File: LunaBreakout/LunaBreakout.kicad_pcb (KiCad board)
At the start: 2 copper layers, 62 parts, among them J1 Conn_01x03, J10 Conn_01x02, J11 Conn_01x03, J12 Conn_01x03, J13 Conn_01x04, J14 Conn_01x04, J15 5 V BEC, J16 GND, J17 Conn_01x04, J18 Conn_01x04, J19 Conn_01x04, J2 Conn_01x03, J3 Conn_01x04, J4 Conn_01x03, J5 Conn_01x03, J6 USB_C_Receptacle_USB2.0_16P, J8 Conn_01x04, J9 Conn_01x04, SW1 SW_SPST, U1 RP2040, U2 AMS1117-3.3, U3 W25Q32JVSS, U4 ISO7721D, U5 ISO7720D, U8 ISO7741DBQ, Y1 12Mhz

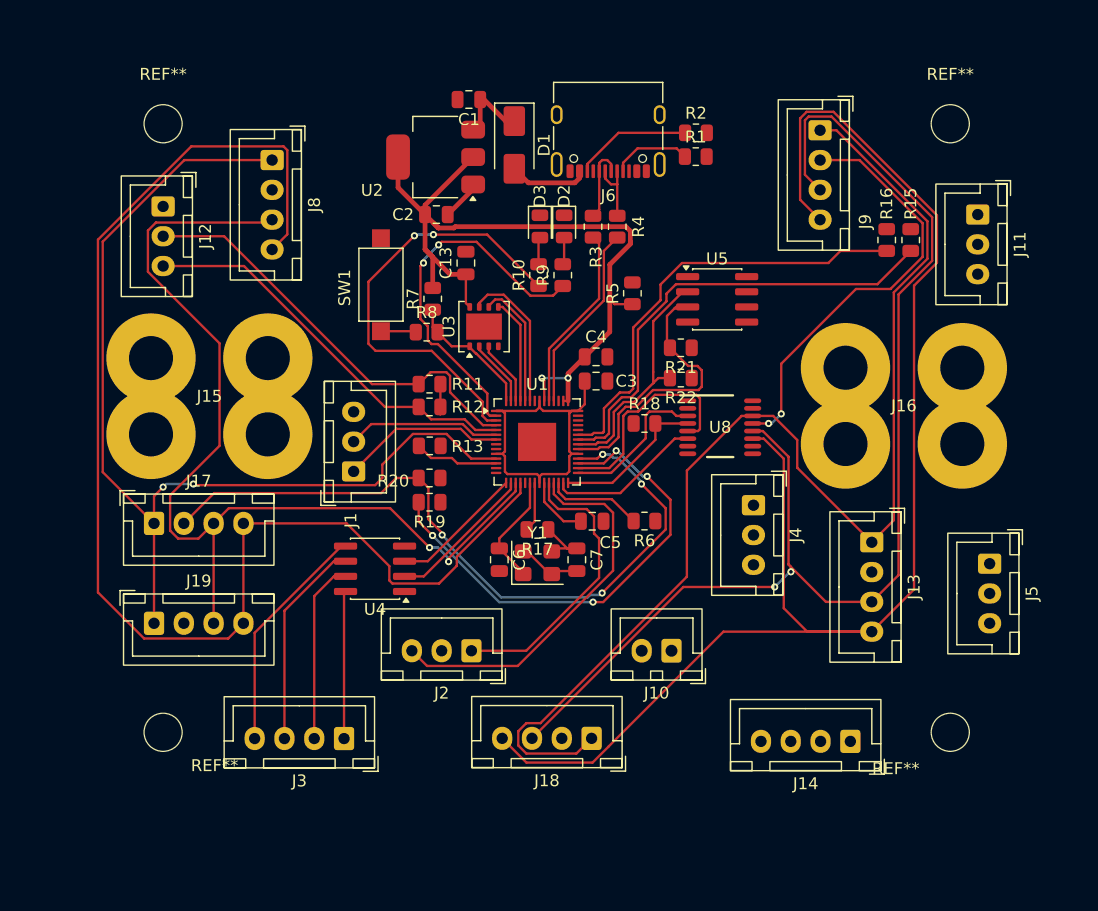
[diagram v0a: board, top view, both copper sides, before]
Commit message: Routed traces, 5 DRC errors that aren't real, still needs silkscreen labels
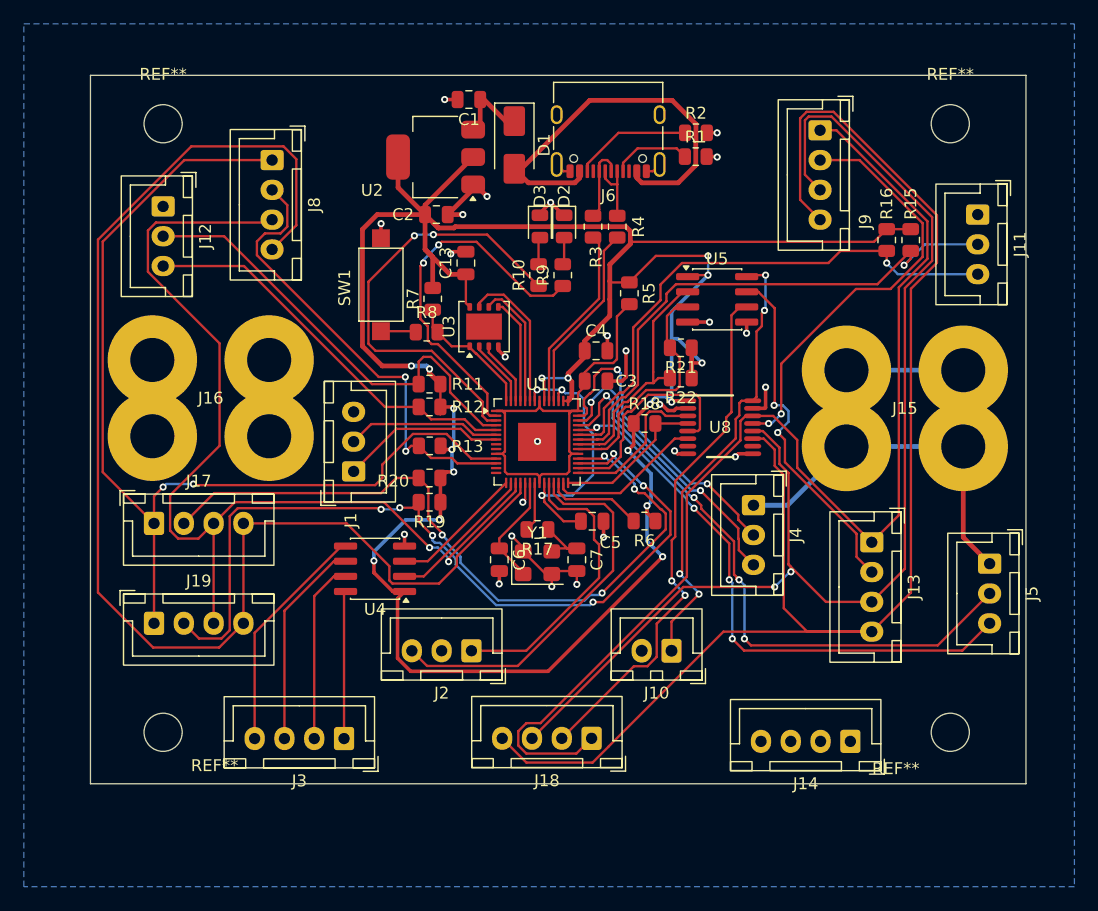
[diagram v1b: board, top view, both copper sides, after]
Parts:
- moved J15 58.4 mm to (238.2, 85.0)
- moved J16 58.2 mm to (179.9, 84.1)
- moved C4 0.51 mm to (217.2, 77.0)
- moved R5 0.25 mm to (220.0, 72.1), turned to -90 degrees
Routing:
- net +3.3V: track 70.0 -> 224.1 mm, vias 2 -> 17
- net GP27/ADC1: track 0.00 -> 52.1 mm, vias 0 -> 4
- net GP26/ADC0: track 0.00 -> 48.3 mm, vias 0 -> 4
- net Net-(J18-Pin_2): track 0.00 -> 44.5 mm, vias 0 -> 2
- net GND: track 28.3 -> 69.0 mm, vias 0 -> 25
- net +5VA: track 0.00 -> 40.2 mm
- net Net-(J10-Pin_1): track 0.00 -> 38.3 mm, vias 0 -> 4
- net GP9 SPI1_CS: track 7.09 -> 39.1 mm, vias 0 -> 2
- net GP20: track 40.9 -> 71.9 mm, vias 4 -> 6
- net Net-(J13-Pin_2): track 0.00 -> 29.6 mm, vias 0 -> 2
- net Net-(D1-A): track 6.71 -> 34.9 mm
- net GP29/ADC3: track 0.00 -> 25.7 mm, vias 0 -> 2
- net GP28/ADC2: track 0.00 -> 24.7 mm, vias 0 -> 2
- net Net-(U1-VREG_VOUT): track 5.34 -> 23.6 mm, vias 0 -> 3
- net Net-(C3-Pad1): track 29.5 -> 38.4 mm
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- added copper zone on B.Cu, net GND
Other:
- board outline added: 78.5 x 59.4 mm
